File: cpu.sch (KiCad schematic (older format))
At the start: 16 parts, among them J1 Conn_02x05_Odd_Even, SW2 SW_Push, SW3 SW_Push, U1 E73-2G4M04S-52832

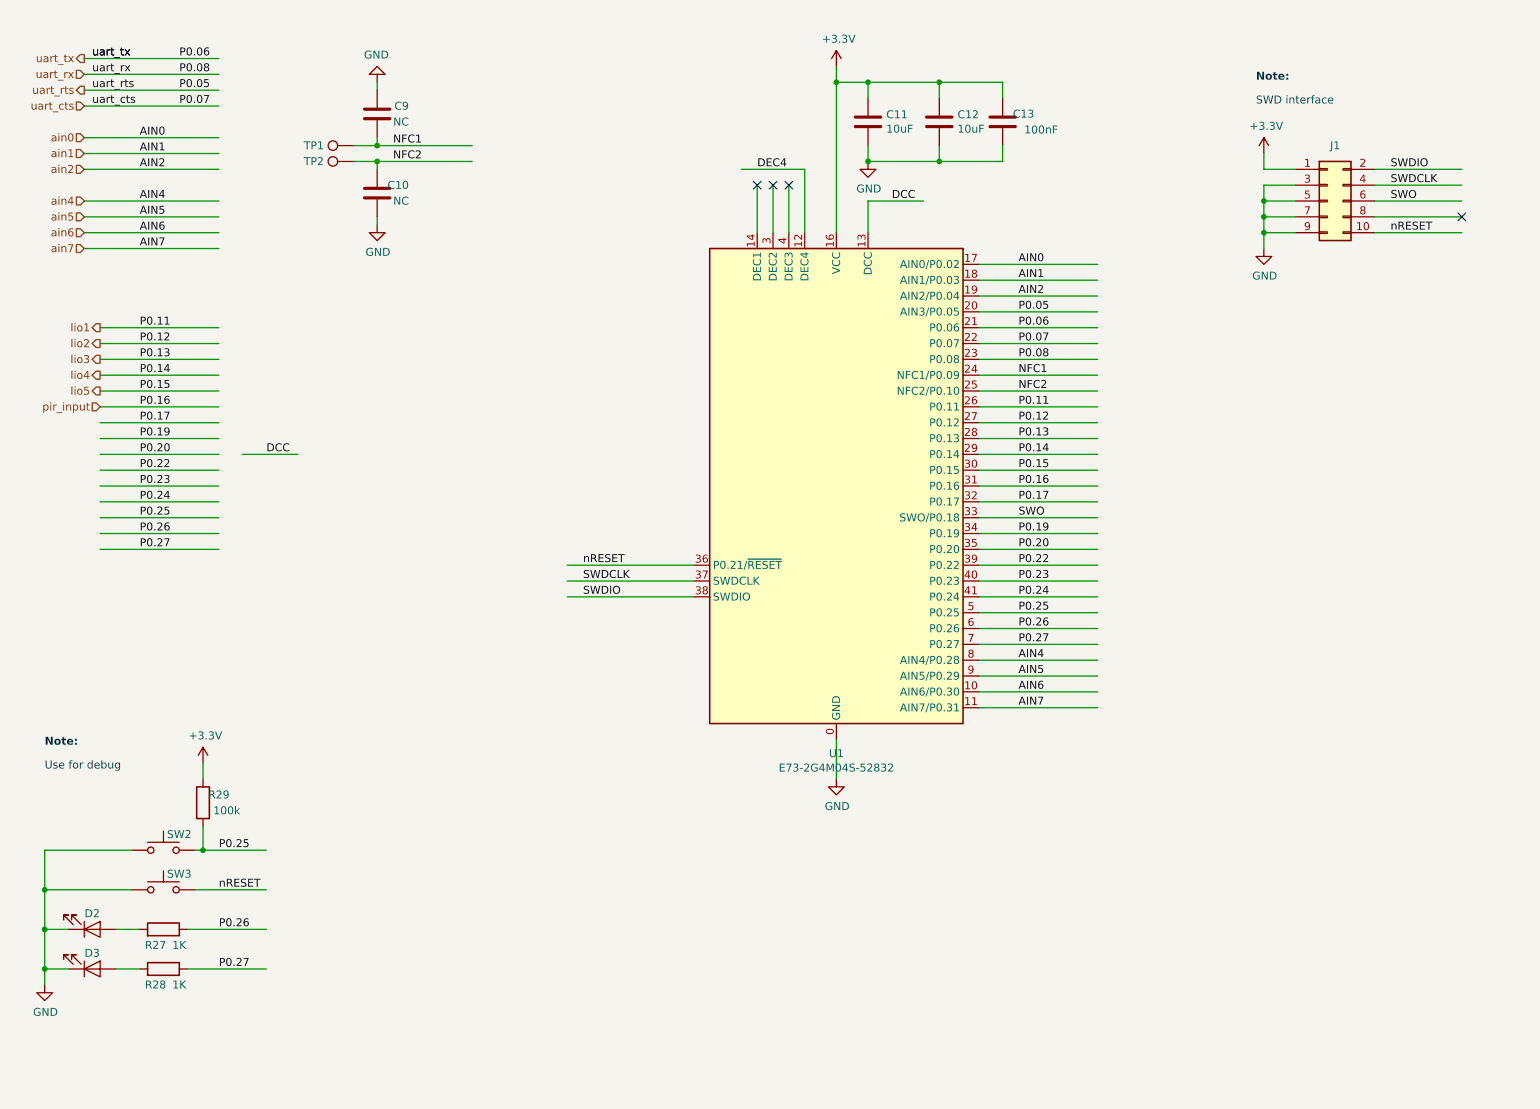
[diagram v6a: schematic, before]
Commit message: layout and more silk informations
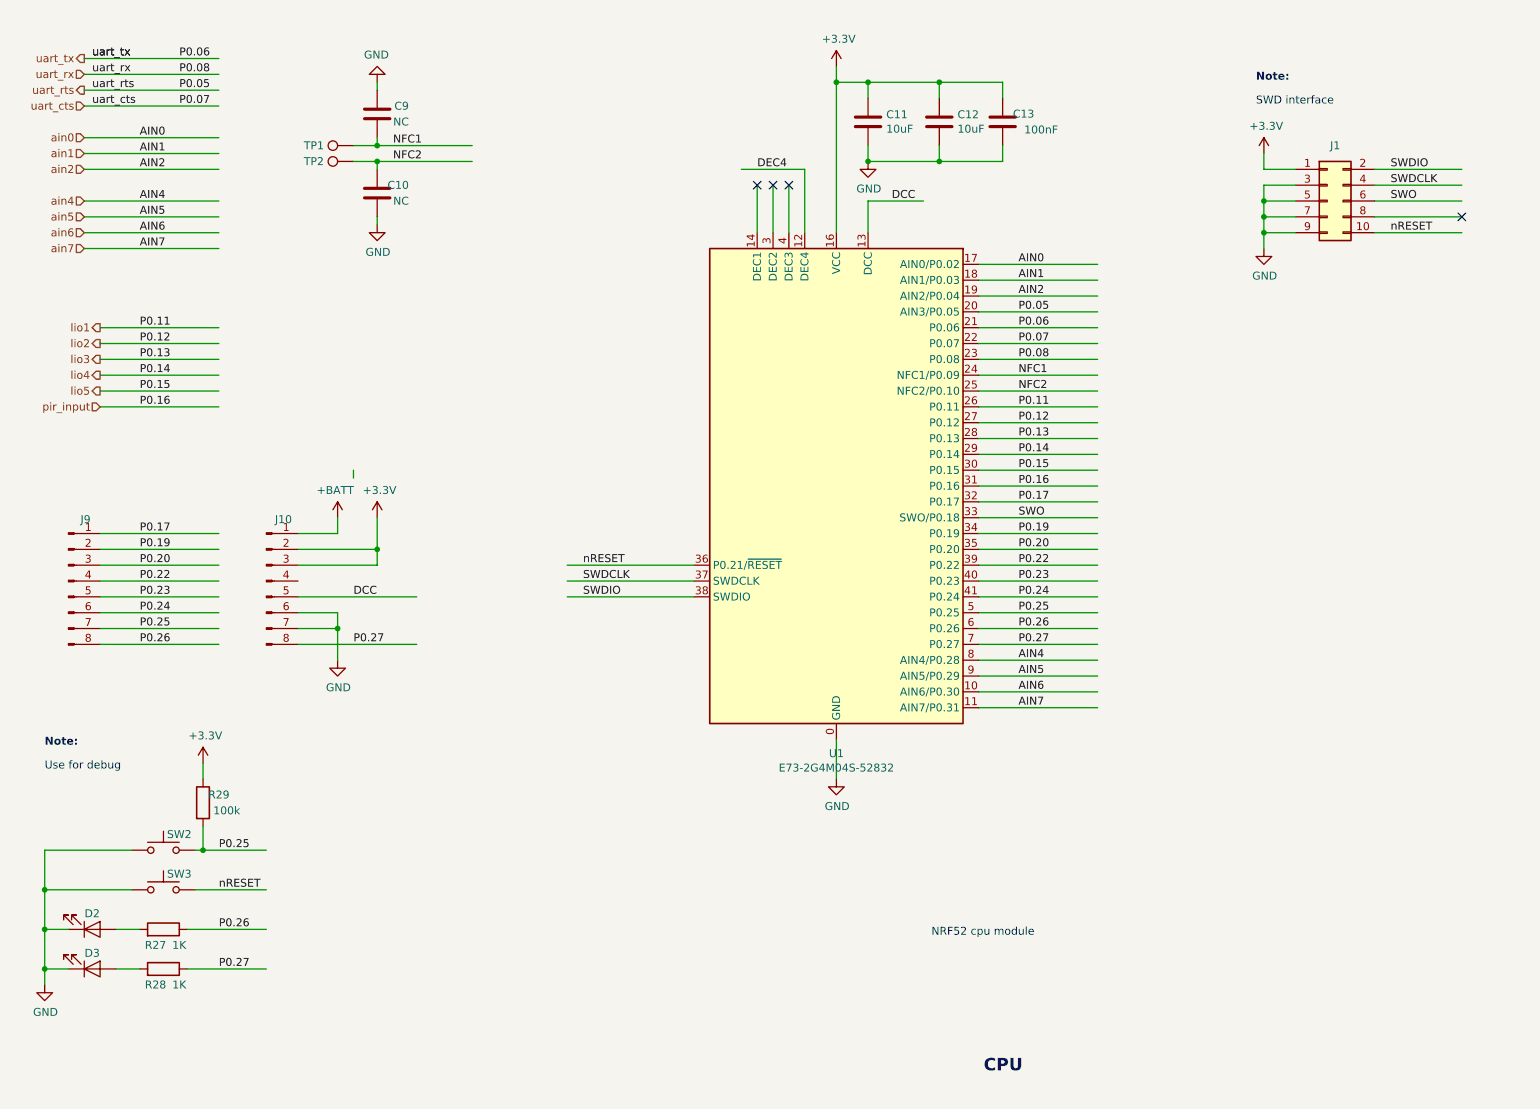
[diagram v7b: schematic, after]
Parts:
- added J10, J9: Conn_01x08_Male, Connector_PinHeader_2.54mm:PinHeader_1x08_P2.54mm_Vertical_SMD_Pin1Left, symbol Connector:Conn_01x08_Male
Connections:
- net labels added: +BATT
- wire segments 120 -> 131
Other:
- note added: "CPU"
- note added: "NRF52 cpu module"
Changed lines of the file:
@@
 	2500 3300 1750 3300
 Wire Wire Line
-	2500 3500 1750 3500
-Wire Wire Line
-	2500 3600 1750 3600
-Wire Wire Line
-	2500 3700 1750 3700
-Wire Wire Line
-	2500 3800 1750 3800
-Wire Wire Line
-	2500 3900 1750 3900
-Wire Wire Line
-	2500 4000 1750 4000
-Wire Wire Line
-	2500 4100 1750 4100
-Wire Wire Line
 	2500 4200 1750 4200
+Wire Wire Line
+	2500 4300 1750 4300
+Wire Wire Line
+	2500 4400 1750 4400
+Wire Wire Line
+	2500 4500 1750 4500
+Wire Wire Line
+	2500 4600 1750 4600
+Wire Wire Line
+	2500 4700 1750 4700
+Wire Wire Line
+	2500 4800 1750 4800
+Wire Wire Line
+	3750 4800 3000 4800
 Text Label 3600 1650 0    50   ~ 0
 NFC1
@@
 Text Label 2000 3300 0    50   ~ 0
 P0.16
-Text Label 2000 3600 0    50   ~ 0
+Text Label 2000 4300 0    50   ~ 0
 P0.20
-Text Label 2000 3700 0    50   ~ 0
+Text Label 2000 4400 0    50   ~ 0
 P0.22
-Text Label 2000 3800 0    50   ~ 0
+Text Label 2000 4500 0    50   ~ 0
 P0.23
-Text Label 2000 3900 0    50   ~ 0
+Text Label 2000 4600 0    50   ~ 0
 P0.24
-Text Label 2000 4000 0    50   ~ 0
+Text Label 2000 4700 0    50   ~ 0
 P0.25
+Text Label 2000 4800 0    50   ~ 0
+P0.26
+Text Label 3350 4800 0    50   ~ 0
+P0.27
+Text Label 2000 4200 0    50   ~ 0
+P0.19
 Text Label 2000 4100 0    50   ~ 0
-P0.26
-Text Label 2000 4200 0    50   ~ 0
-P0.27
-Text Label 2000 3500 0    50   ~ 0
-P0.19
-Text Label 2000 3400 0    50   ~ 0
 P0.17
 Wire Wire Line
-	2500 3400 1750 3400
+	2500 4100 1750 4100
 Text HLabel 1750 2800 0    50   Output ~ 0
 lio1
@@
 $EndComp
 Wire Wire Line
-	2650 3600 3000 3600
-Text Label 2800 3600 0    50   ~ 0
+	3000 4500 3750 4500
+Text Label 3350 4500 0    50   ~ 0
 DCC
 Wire Wire Line
@@
 Connection ~ 3500 1650
 Connection ~ 3500 1750
+Text Notes 7330 7510 0    79   ~ 16
+CPU
+Text Notes 7000 6650 0    50   ~ 0
+NRF52 cpu module
+$Comp
+L power:GND #PWR0138
+U 1 1 5E9CE3E9
+P 3250 4900
+F 0 "#PWR0138" H 3250 4650 50  0001 C CNN
+F 1 "GND" H 3255 4727 50  0000 C CNN
+F 2 "" H 3250 4900 50  0001 C CNN
+F 3 "" H 3250 4900 50  0001 C CNN
+	1    3250 4900
+	1    0    0    -1
+$EndComp
+Wire Wire Line
+	3350 3700 3350 3750
+$Comp
+L power:+3.3V #PWR?
+U 1 1 5E9D3C0C
+P 3500 4000
+AR Path="/5E9D3C0C" Ref="#PWR?"  Part="1"
+AR Path="/5E59E010/5E9D3C0C" Ref="#PWR0139"  Part="1"
+F 0 "#PWR0139" H 3500 3850 50  0001 C CNN
+F 1 "+3.3V" H 3515 4173 50  0000 C CNN
+F 2 "" H 3500 4000 50  0001 C CNN
+F 3 "" H 3500 4000 50  0001 C CNN
+	1    3500 4000
+	1    0    0    -1
+$EndComp
+$Comp
+L power:+BATT #PWR?
+U 1 1 5E9D9A21
+P 3250 4000
+AR Path="/5E5BC499/5E9D9A21" Ref="#PWR?"  Part="1"
+AR Path="/5E59E010/5E9D9A21" Ref="#PWR0140"  Part="1"
+F 0 "#PWR0140" H 3250 3850 50  0001 C CNN
+F 1 "+BATT" H 3265 4173 50  0000 C CNN
+F 2 "" H 3250 4000 50  0001 C CNN
+F 3 "" H 3250 4000 50  0001 C CNN
+	1    3250 4000
+	-1   0    0    -1
+$EndComp
+$Comp
+L Connector:Conn_01x08_Male J9
+U 1 1 5E9F0561
+P 1550 4400
+F 0 "J9" H 1658 4789 50  0000 C CNN
+F 1 "Conn_01x08_Male" H 1658 4790 50  0001 C CNN
+F 2 "Connector_PinHeader_2.54mm:PinHeader_1x08_P2.54mm_Vertical_SMD_Pin1Left" H 1550 4400 50  0001 C CNN
+F 3 "~" H 1550 4400 50  0001 C CNN
+	1    1550 4400
+	1    0    0    -1
+$EndComp
+Wire Wire Line
+	3250 4900 3250 4700
+Wire Wire Line
+	3250 4700 3000 4700
+Wire Wire Line
+	3000 4600 3250 4600
+Wire Wire Line
+	3250 4600 3250 4700
+Connection ~ 3250 4700
+Wire Wire Line
+	3250 4000 3250 4100
+Wire Wire Line
+	3250 4100 3000 4100
+$Comp
+L Connector:Conn_01x08_Male J10
+U 1 1 5EA01F00
+P 2800 4400
+F 0 "J10" H 2908 4789 50  0000 C CNN
+F 1 "Conn_01x08_Male" H 2908 4790 50  0001 C CNN
+F 2 "Connector_PinHeader_2.54mm:PinHeader_1x08_P2.54mm_Vertical_SMD_Pin1Left" H 2800 4400 50  0001 C CNN
+F 3 "~" H 2800 4400 50  0001 C CNN
+	1    2800 4400
+	1    0    0    -1
+$EndComp
+Wire Wire Line
+	3000 4200 3500 4200
+Wire Wire Line
+	3000 4300 3500 4300
+Wire Wire Line
+	3500 4000 3500 4200
+Connection ~ 3500 4200
+Wire Wire Line
+	3500 4200 3500 4300
 $EndSCHEMATC

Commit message: finished layout, created production files and added readme
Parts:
- C11, C12: LCSC (none) -> C13585; MPN (none) -> CL31A106KBHNNNE
- C13: LCSC (none) -> C28233; MPN (none) -> CL21B104KCFNNNE
- D2, D3: LCSC (none) -> C72043; MPN (none) -> 19-217/GHC-YR1S2/3T
- R27, R28: value 1K -> 1k; LCSC (none) -> C17513; MPN (none) -> 0805W8F1001T5E
- R29: LCSC (none) -> C17407; MPN (none) -> 0805W8F1003T5E
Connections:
- net labels removed: ain5, ain6, ain7
- wire segments 131 -> 126
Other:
- note added: "1.0"
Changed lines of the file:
@@
 AIN0
 Wire Wire Line
-	2500 2000 1650 2000
-Wire Wire Line
-	2500 2100 1650 2100
-Wire Wire Line
-	2500 2200 1650 2200
-Wire Wire Line
-	2500 2300 1650 2300
-Text Label 2000 2000 0    50   ~ 0
+	2500 1910 1650 1910
+Text Label 2000 1910 0    50   ~ 0
 AIN4
-Text Label 2000 2100 0    50   ~ 0
+Text Label 3375 4200 0    50   ~ 0
 AIN5
-Text Label 2000 2200 0    50   ~ 0
+Text Label 3350 4400 0    50   ~ 0
 AIN6
-Text Label 2000 2300 0    50   ~ 0
+Text Label 3350 4600 0    50   ~ 0
 AIN7
 Text HLabel 1650 1600 0    50   Input ~ 0
@@
 Text HLabel 1650 1800 0    50   Input ~ 0
 ain2
-Text HLabel 1650 2000 0    50   Input ~ 0
+Text HLabel 1650 1910 0    50   Input ~ 0
 ain4
-Text HLabel 1650 2100 0    50   Input ~ 0
-ain5
-Text HLabel 1650 2200 0    50   Input ~ 0
-ain6
-Text HLabel 1650 2300 0    50   Input ~ 0
-ain7
 Wire Wire Line
 	2500 2800 1750 2800
@@
 F 2 "LED_SMD:LED_0603_1608Metric_Pad1.05x0.95mm_HandSolder" H 1700 6850 50  0001 C CNN
 F 3 "~" H 1700 6850 50  0001 C CNN
+F 4 "19-217/GHC-YR1S2/3T" H 1700 6850 50  0001 C CNN "MPN"
+F 5 "C72043" H 1700 6850 50  0001 C CNN "LCSC"
 	1    1700 6850
 	1    0    0    1
@@
 AR Path="/5E59E010/5E9D5866" Ref="R28"  Part="1"
 F 0 "R28" V 2050 6800 50  0000 C CNN
-F 1 "1K" V 2050 6950 50  0000 C CNN
+F 1 "1k" V 2050 6950 50  0000 C CNN
 F 2 "Resistor_SMD:R_0805_2012Metric_Pad1.15x1.40mm_HandSolder" V 2080 6850 50  0001 C CNN
 F 3 "~" H 2150 6850 50  0001 C CNN
+F 4 "0805W8F1001T5E" H 2150 6850 50  0001 C CNN "MPN"
+F 5 "C17513" H 2150 6850 50  0001 C CNN "LCSC"
 	1    2150 6850
 	0    1    -1   0
@@
 F 2 "LED_SMD:LED_0603_1608Metric_Pad1.05x0.95mm_HandSolder" H 1700 6600 50  0001 C CNN
 F 3 "~" H 1700 6600 50  0001 C CNN
+F 4 "19-217/GHC-YR1S2/3T" H 1700 6600 50  0001 C CNN "MPN"
+F 5 "C72043" H 1700 6600 50  0001 C CNN "LCSC"
 	1    1700 6600
 	1    0    0    1
@@
 AR Path="/5E59E010/5E9EB508" Ref="R27"  Part="1"
 F 0 "R27" V 2050 6550 50  0000 C CNN
-F 1 "1K" V 2050 6700 50  0000 C CNN
+F 1 "1k" V 2050 6700 50  0000 C CNN
 F 2 "Resistor_SMD:R_0805_2012Metric_Pad1.15x1.40mm_HandSolder" V 2080 6600 50  0001 C CNN
 F 3 "~" H 2150 6600 50  0001 C CNN
+F 4 "0805W8F1001T5E" H 2150 6600 50  0001 C CNN "MPN"
+F 5 "C17513" H 2150 6600 50  0001 C CNN "LCSC"
 	1    2150 6600
 	0    1    -1   0
@@
 F 2 "Resistor_SMD:R_0805_2012Metric_Pad1.15x1.40mm_HandSolder" V 2330 5800 50  0001 C CNN
 F 3 "~" H 2400 5800 50  0001 C CNN
+F 4 "0805W8F1003T5E" H 2400 5800 50  0001 C CNN "MPN"
+F 5 "C17407" H 2400 5800 50  0001 C CNN "LCSC"
 	1    2400 5800
 	1    0    0    -1
@@
 F 2 "Capacitor_SMD:C_1210_3225Metric_Pad1.42x2.65mm_HandSolder" H 6638 1350 50  0001 C CNN
 F 3 "~" H 6600 1500 50  0001 C CNN
+F 4 "CL31A106KBHNNNE" H 6600 1500 50  0001 C CNN "MPN"
+F 5 "C13585" H 6600 1500 50  0001 C CNN "LCSC"
 	1    6600 1500
 	1    0    0    -1
@@
 F 2 "Capacitor_SMD:C_1210_3225Metric_Pad1.42x2.65mm_HandSolder" H 7088 1350 50  0001 C CNN
 F 3 "~" H 7050 1500 50  0001 C CNN
+F 4 "CL31A106KBHNNNE" H 7050 1500 50  0001 C CNN "MPN"
+F 5 "C13585" H 7050 1500 50  0001 C CNN "LCSC"
 	1    7050 1500
 	1    0    0    -1
@@
 AR Path="/5E8399F7/5E983FD2" Ref="C?"  Part="1"
 AR Path="/5E59E010/5E983FD2" Ref="C13"  Part="1"
-F 0 "C13" H 7250 1450 50  0000 L CNN
+F 0 "C13" H 7200 1450 50  0000 L CNN
 F 1 "100nF" H 7100 1550 50  0000 L CNN
 F 2 "Capacitor_SMD:C_0805_2012Metric_Pad1.15x1.40mm_HandSolder" H 7488 1350 50  0001 C CNN
 F 3 "~" H 7450 1500 50  0001 C CNN
+F 4 "CL21B104KCFNNNE" H 7450 1500 50  0001 C CNN "MPN"
+F 5 "C28233" H 7450 1500 50  0001 C CNN "LCSC"
 	1    7450 1500
 	-1   0    0    1
@@
 	1    0    0    -1
 $EndComp
-Wire Wire Line
-	3350 3700 3350 3750
 $Comp
 L power:+3.3V #PWR?
 U 1 1 5E9D3C0C
-P 3500 4000
+P 3675 4000
 AR Path="/5E9D3C0C" Ref="#PWR?"  Part="1"
 AR Path="/5E59E010/5E9D3C0C" Ref="#PWR0139"  Part="1"
-F 0 "#PWR0139" H 3500 3850 50  0001 C CNN
-F 1 "+3.3V" H 3515 4173 50  0000 C CNN
-F 2 "" H 3500 4000 50  0001 C CNN
-F 3 "" H 3500 4000 50  0001 C CNN
-	1    3500 4000
+F 0 "#PWR0139" H 3675 3850 50  0001 C CNN
+F 1 "+3.3V" H 3690 4173 50  0000 C CNN
+F 2 "" H 3675 4000 50  0001 C CNN
+F 3 "" H 3675 4000 50  0001 C CNN
+	1    3675 4000
 	1    0    0    -1
 $EndComp
@@
 	3250 4700 3000 4700
 Wire Wire Line
-	3000 4600 3250 4600
-Wire Wire Line
-	3250 4600 3250 4700
-Connection ~ 3250 4700
-Wire Wire Line
 	3250 4000 3250 4100
 Wire Wire Line
 	3250 4100 3000 4100
+Wire Wire Line
+	3750 4200 3000 4200
+Wire Wire Line
+	3750 4400 3000 4400
+Wire Wire Line
+	3750 4600 3000 4600
 $Comp
 L Connector:Conn_01x08_Male J10
@@
 $EndComp
 Wire Wire Line
-	3000 4200 3500 4200
-Wire Wire Line
-	3000 4300 3500 4300
-Wire Wire Line
-	3500 4000 3500 4200
-Connection ~ 3500 4200
-Wire Wire Line
-	3500 4200 3500 4300
+	3000 4300 3675 4300
+Wire Wire Line
+	3675 4300 3675 4000
+Text Notes 10600 7640 0    50   ~ 0
+1.0
 $EndSCHEMATC
